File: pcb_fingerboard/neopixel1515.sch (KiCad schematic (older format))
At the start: 123 parts, among them J1 Conn_01x03

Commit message: Pre-print fingerboard pcb
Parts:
- added H1, H2, H3, H4: MountingHole, MountingHole:MountingHole_3.2mm_M3, symbol Mechanical:MountingHole
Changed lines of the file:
@@
 Wire Wire Line
 	32500 7800 32850 7800
+$Comp
+L Mechanical:MountingHole H1
+U 1 1 6184DABC
+P 36650 1550
+F 0 "H1" H 36750 1596 50  0000 L CNN
+F 1 "MountingHole" H 36750 1505 50  0000 L CNN
+F 2 "MountingHole:MountingHole_3.2mm_M3" H 36650 1550 50  0001 C CNN
+F 3 "~" H 36650 1550 50  0001 C CNN
+	1    36650 1550
+	1    0    0    -1
+$EndComp
+$Comp
+L Mechanical:MountingHole H3
+U 1 1 61DD112F
+P 36650 1850
+F 0 "H3" H 36750 1896 50  0000 L CNN
+F 1 "MountingHole" H 36750 1805 50  0000 L CNN
+F 2 "MountingHole:MountingHole_3.2mm_M3" H 36650 1850 50  0001 C CNN
+F 3 "~" H 36650 1850 50  0001 C CNN
+	1    36650 1850
+	1    0    0    -1
+$EndComp
+$Comp
+L Mechanical:MountingHole H2
+U 1 1 61E9A2F3
+P 37500 1550
+F 0 "H2" H 37600 1596 50  0000 L CNN
+F 1 "MountingHole" H 37600 1505 50  0000 L CNN
+F 2 "MountingHole:MountingHole_3.2mm_M3" H 37500 1550 50  0001 C CNN
+F 3 "~" H 37500 1550 50  0001 C CNN
+	1    37500 1550
+	1    0    0    -1
+$EndComp
+$Comp
+L Mechanical:MountingHole H4
+U 1 1 61F6323C
+P 37500 1850
+F 0 "H4" H 37600 1896 50  0000 L CNN
+F 1 "MountingHole" H 37600 1805 50  0000 L CNN
+F 2 "MountingHole:MountingHole_3.2mm_M3" H 37500 1850 50  0001 C CNN
+F 3 "~" H 37500 1850 50  0001 C CNN
+	1    37500 1850
+	1    0    0    -1
+$EndComp
 $EndSCHEMATC

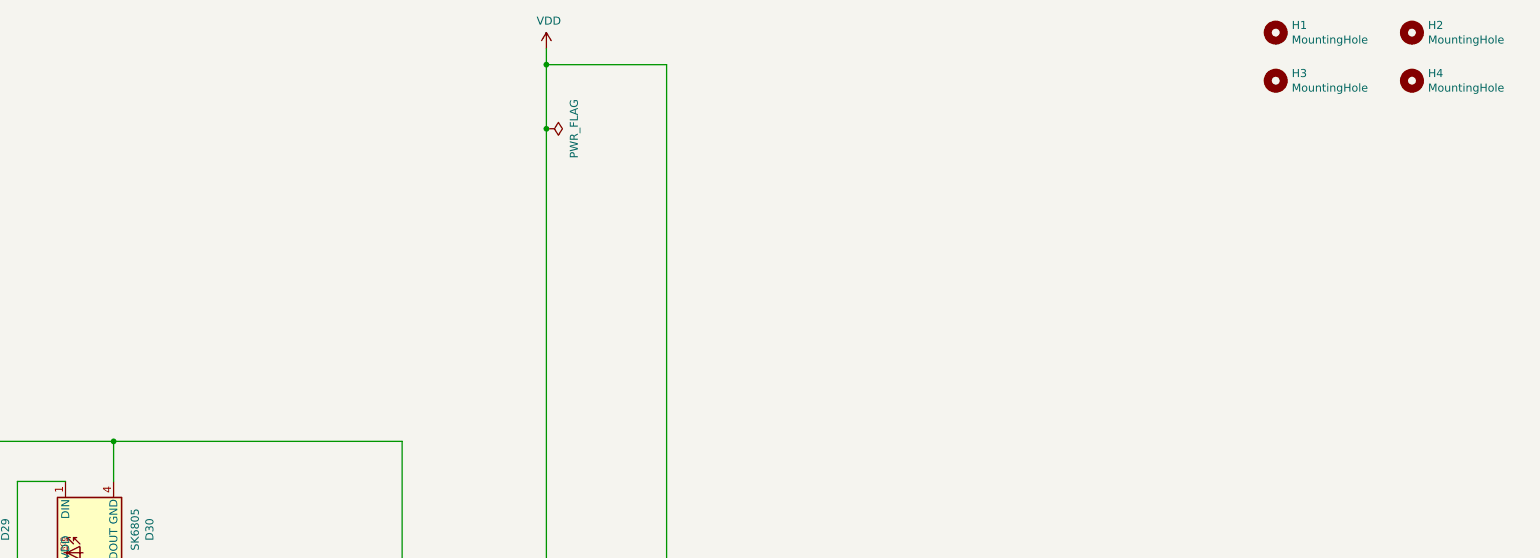
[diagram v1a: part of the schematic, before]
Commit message: Added padded mounting holes with vias
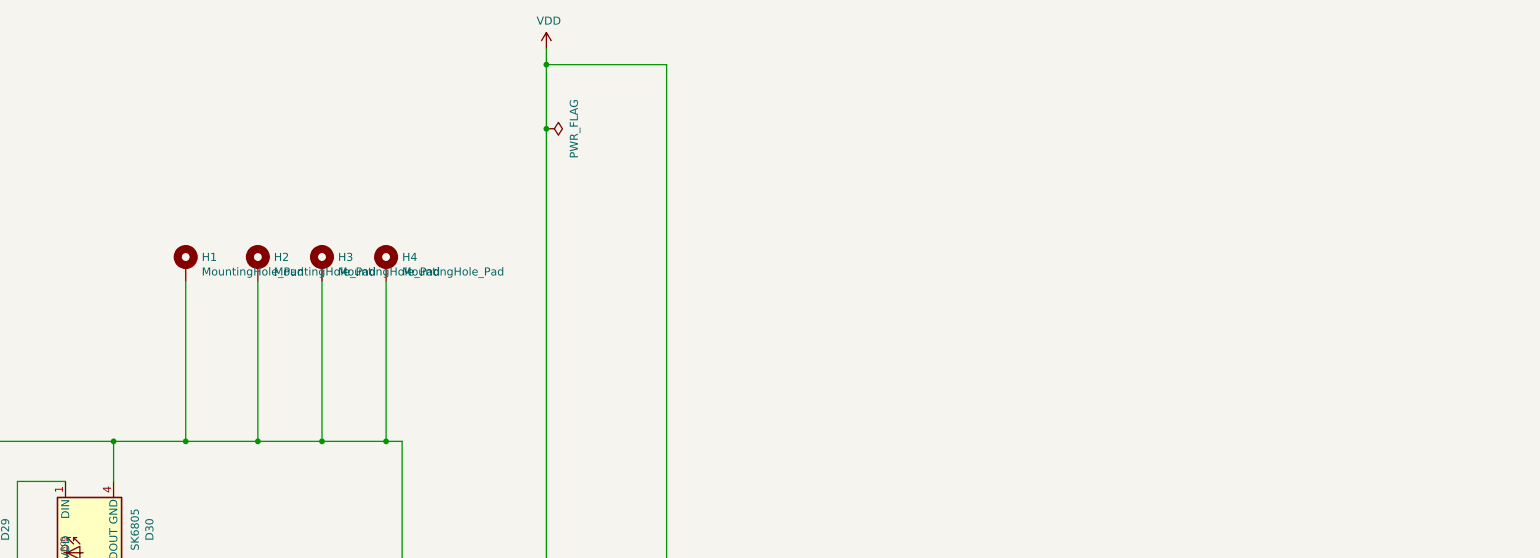
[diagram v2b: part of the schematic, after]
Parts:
- removed H1, H2, H3, H4: MountingHole, MountingHole:MountingHole_3.2mm_M3, symbol Mechanical:MountingHole
- added H1, H2, H3, H4: MountingHole_Pad, MountingHole:MountingHole_3.2mm_M3_Pad_Via, symbol Mechanical:MountingHole_Pad
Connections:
- net GND: now also H1.1, H2.1, H3.1, H4.1
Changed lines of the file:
@@
 Wire Wire Line
 	31200 6350 31200 6400
-Wire Wire Line
-	29400 4100 31200 4100
 Connection ~ 29400 4100
 Wire Wire Line
@@
 Wire Wire Line
 	32500 7800 32850 7800
-$Comp
-L Mechanical:MountingHole H1
-U 1 1 6184DABC
-P 36650 1550
-F 0 "H1" H 36750 1596 50  0000 L CNN
-F 1 "MountingHole" H 36750 1505 50  0000 L CNN
-F 2 "MountingHole:MountingHole_3.2mm_M3" H 36650 1550 50  0001 C CNN
-F 3 "~" H 36650 1550 50  0001 C CNN
-	1    36650 1550
+Wire Wire Line
+	29400 4100 29850 4100
+$Comp
+L Mechanical:MountingHole_Pad H2
+U 1 1 60EB64CB
+P 30300 3000
+F 0 "H2" H 30400 3049 50  0000 L CNN
+F 1 "MountingHole_Pad" H 30400 2958 50  0000 L CNN
+F 2 "MountingHole:MountingHole_3.2mm_M3_Pad_Via" H 30300 3000 50  0001 C CNN
+F 3 "~" H 30300 3000 50  0001 C CNN
+	1    30300 3000
 	1    0    0    -1
 $EndComp
 $Comp
-L Mechanical:MountingHole H3
-U 1 1 61DD112F
-P 36650 1850
-F 0 "H3" H 36750 1896 50  0000 L CNN
-F 1 "MountingHole" H 36750 1805 50  0000 L CNN
-F 2 "MountingHole:MountingHole_3.2mm_M3" H 36650 1850 50  0001 C CNN
-F 3 "~" H 36650 1850 50  0001 C CNN
-	1    36650 1850
+L Mechanical:MountingHole_Pad H3
+U 1 1 6104C008
+P 30700 3000
+F 0 "H3" H 30800 3049 50  0000 L CNN
+F 1 "MountingHole_Pad" H 30800 2958 50  0000 L CNN
+F 2 "MountingHole:MountingHole_3.2mm_M3_Pad_Via" H 30700 3000 50  0001 C CNN
+F 3 "~" H 30700 3000 50  0001 C CNN
+	1    30700 3000
 	1    0    0    -1
 $EndComp
 $Comp
-L Mechanical:MountingHole H2
-U 1 1 61E9A2F3
-P 37500 1550
-F 0 "H2" H 37600 1596 50  0000 L CNN
-F 1 "MountingHole" H 37600 1505 50  0000 L CNN
-F 2 "MountingHole:MountingHole_3.2mm_M3" H 37500 1550 50  0001 C CNN
-F 3 "~" H 37500 1550 50  0001 C CNN
-	1    37500 1550
+L Mechanical:MountingHole_Pad H4
+U 1 1 61114F2B
+P 31100 3000
+F 0 "H4" H 31200 3049 50  0000 L CNN
+F 1 "MountingHole_Pad" H 31200 2958 50  0000 L CNN
+F 2 "MountingHole:MountingHole_3.2mm_M3_Pad_Via" H 31100 3000 50  0001 C CNN
+F 3 "~" H 31100 3000 50  0001 C CNN
+	1    31100 3000
 	1    0    0    -1
 $EndComp
 $Comp
-L Mechanical:MountingHole H4
-U 1 1 61F6323C
-P 37500 1850
-F 0 "H4" H 37600 1896 50  0000 L CNN
-F 1 "MountingHole" H 37600 1805 50  0000 L CNN
-F 2 "MountingHole:MountingHole_3.2mm_M3" H 37500 1850 50  0001 C CNN
-F 3 "~" H 37500 1850 50  0001 C CNN
-	1    37500 1850
+L Mechanical:MountingHole_Pad H1
+U 1 1 611DDF3C
+P 29850 3000
+F 0 "H1" H 29950 3049 50  0000 L CNN
+F 1 "MountingHole_Pad" H 29950 2958 50  0000 L CNN
+F 2 "MountingHole:MountingHole_3.2mm_M3_Pad_Via" H 29850 3000 50  0001 C CNN
+F 3 "~" H 29850 3000 50  0001 C CNN
+	1    29850 3000
 	1    0    0    -1
 $EndComp
+Wire Wire Line
+	29850 3100 29850 4100
+Connection ~ 29850 4100
+Wire Wire Line
+	29850 4100 30300 4100
+Wire Wire Line
+	30300 3100 30300 4100
+Connection ~ 30300 4100
+Wire Wire Line
+	30300 4100 30700 4100
+Wire Wire Line
+	30700 3100 30700 4100
+Connection ~ 30700 4100
+Wire Wire Line
+	30700 4100 31100 4100
+Wire Wire Line
+	31100 3100 31100 4100
+Connection ~ 31100 4100
+Wire Wire Line
+	31100 4100 31200 4100
 $EndSCHEMATC
